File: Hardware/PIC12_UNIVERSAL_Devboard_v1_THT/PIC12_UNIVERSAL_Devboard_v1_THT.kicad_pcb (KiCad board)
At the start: 2 copper layers, 70 x 40 mm, 39 parts, among them J2 Conn_PIC_ICSP_ICD, J3 Screw_Terminal_01x02, J4 Conn_01x07_Pin, SW1 SW_RESET, U1 PIC12F617-xP, U2 78L05G, U3 XC6206-3.3V, U4 SI2301

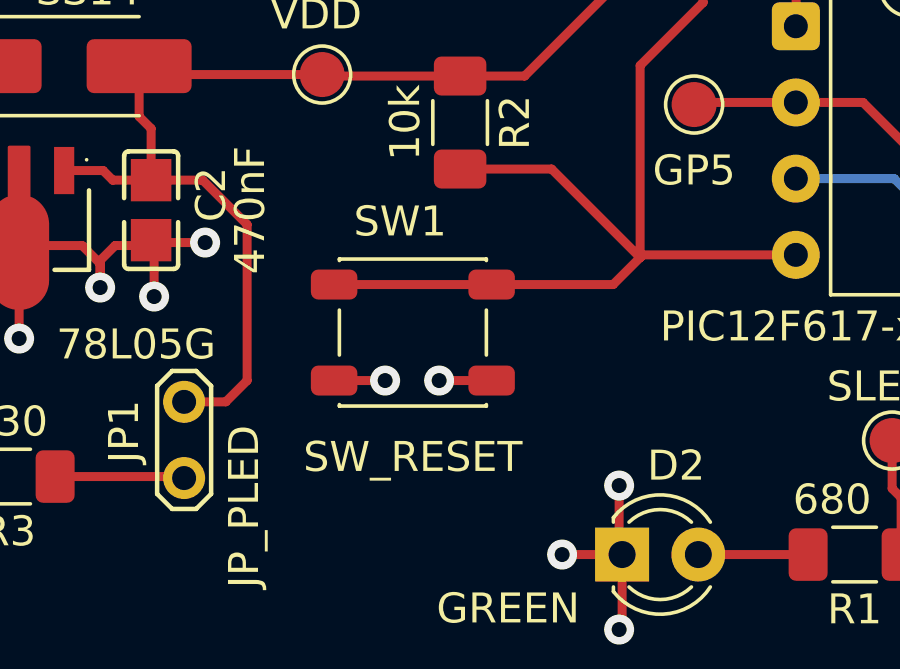
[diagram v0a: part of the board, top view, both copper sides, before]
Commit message: PIC12 Universal Dev Board - Updated Reset Switch Footprint for better Handsoldering
Signed-off-by: alexanderjg85 <alexanderjg85@gmail.com>
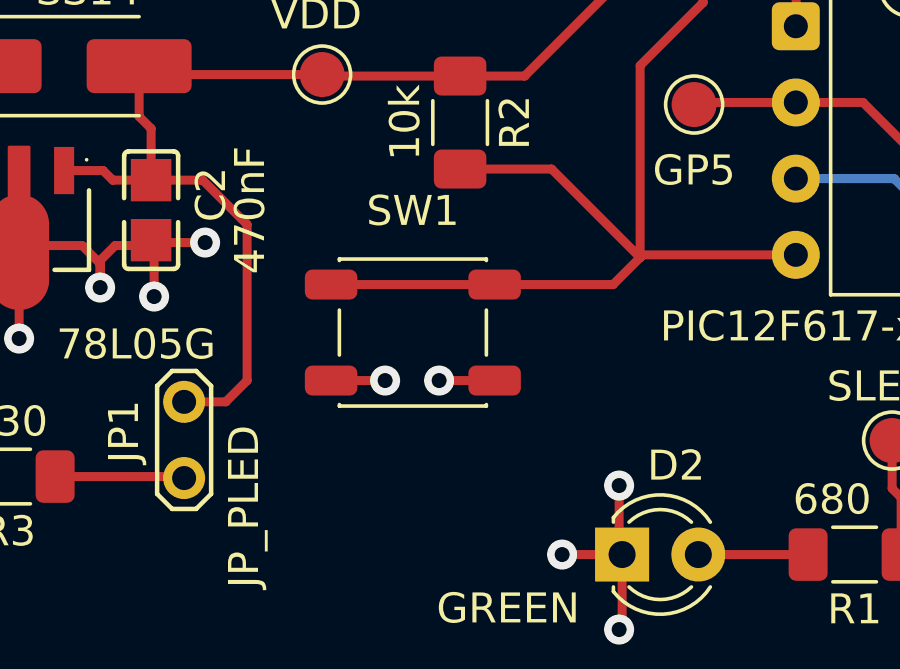
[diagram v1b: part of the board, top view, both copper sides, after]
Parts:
- SW1: footprint Button_Switch_SMD:SW_SPST_PTS647_Sx38 -> AJ_Electromechanical:SW_SPST_PTS647_Sx38_Handsolder
